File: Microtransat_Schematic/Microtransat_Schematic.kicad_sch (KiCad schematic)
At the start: 33 parts, among them IC1 HT7833, M12_Female2 LightTower1, U1 LM2596S-5, U10 RC_Reciever, U5 SD Card Module, U6 SEN0482 Wind Vane, U7 LoRa Module

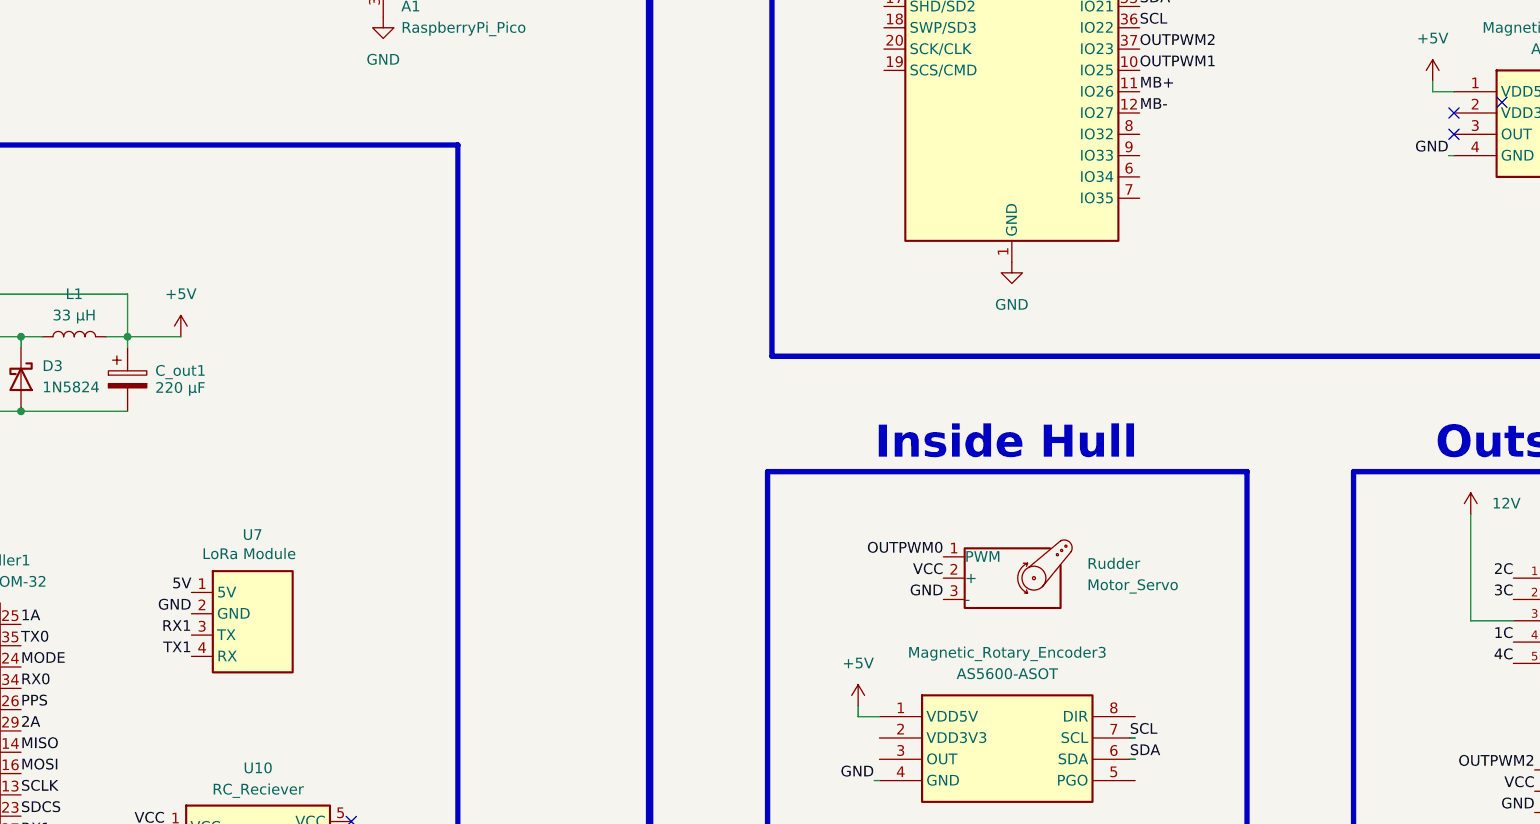
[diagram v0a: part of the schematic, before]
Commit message: Added AS5600 mockup
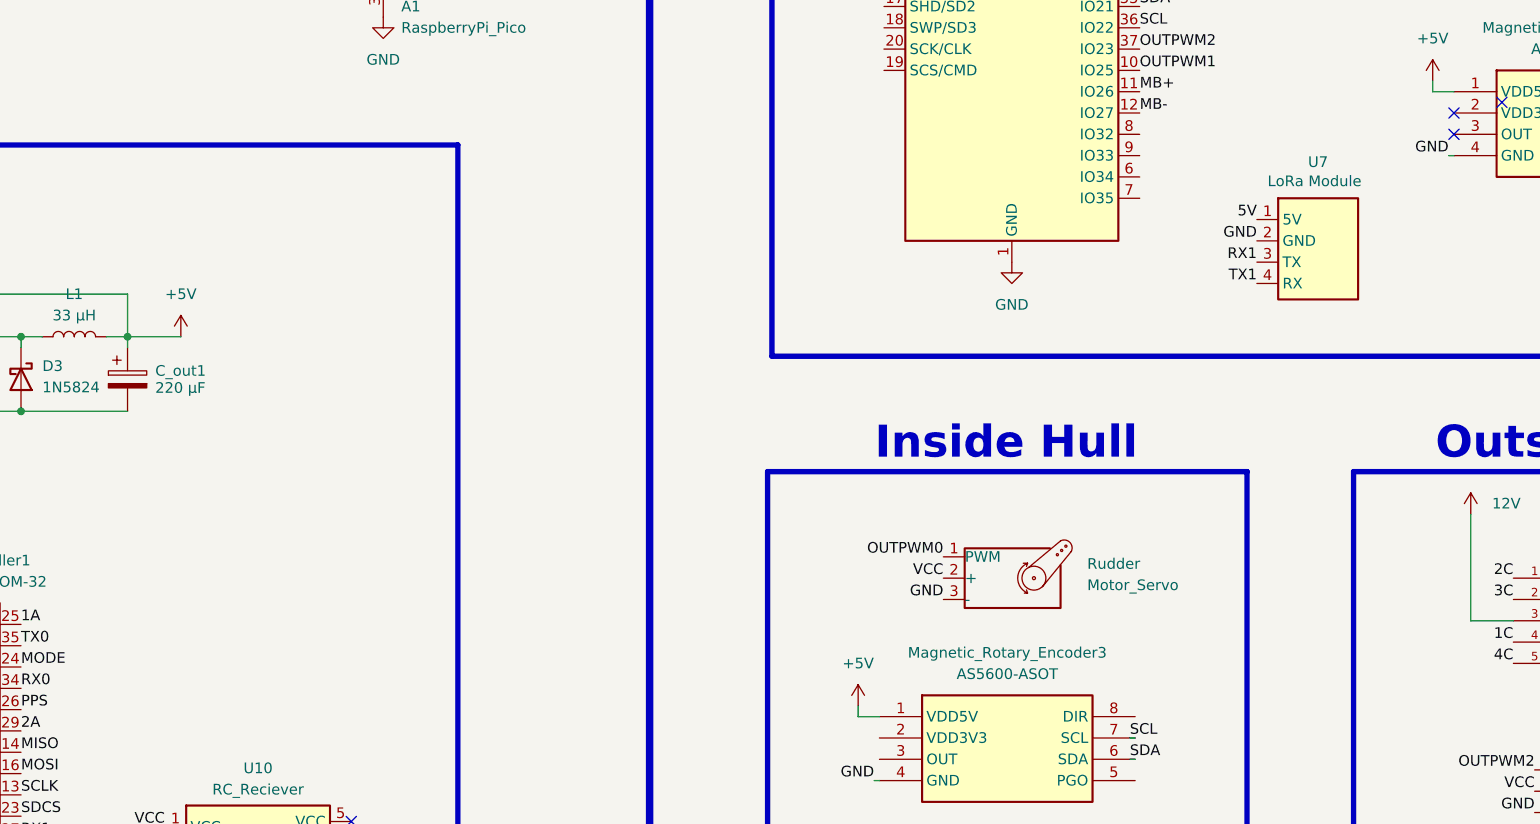
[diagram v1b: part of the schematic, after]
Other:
- moved on the sheet: U7
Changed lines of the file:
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@@
 	)
 	(label "TX1"
-		(at 187.96 193.04 180)
+		(at 314.96 148.59 180)
 		(effects
 			(font
@@
 	)
 	(label "5V"
-		(at 187.96 185.42 180)
+		(at 314.96 140.97 180)
 		(effects
 			(font
@@
 	)
 	(label "GND"
-		(at 187.96 187.96 180)
+		(at 314.96 143.51 180)
 		(effects
 			(font
@@
 	)
 	(label "RX1"
-		(at 187.96 190.5 180)
+		(at 314.96 146.05 180)
 		(effects
 			(font
@@
 	(symbol
 		(lib_id "Microtransat:LoRa Module")
-		(at 196.215 180.34 0)
+		(at 323.215 135.89 0)
 		(unit 1)
 		(exclude_from_sim no)
@@
 		(dnp no)
 		(property "Reference" "U7"
-			(at 194.056 178.562 0)
+			(at 321.056 134.112 0)
 			(effects
 				(font
@@
 		)
 		(property "Value" "LoRa Module"
-			(at 189.23 180.848 0)
+			(at 316.23 136.398 0)
 			(effects
 				(font
@@
 		)
 		(property "Footprint" ""
-			(at 196.215 180.34 0)
+			(at 323.215 135.89 0)
 			(effects
 				(font
@@
 		)
 		(property "Datasheet" ""
-			(at 196.215 180.34 0)
+			(at 323.215 135.89 0)
 			(effects
 				(font
@@
 		)
 		(property "Description" ""
-			(at 196.215 180.34 0)
+			(at 323.215 135.89 0)
 			(effects
 				(font

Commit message: Removed some old/incorrect stuff
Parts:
- removed C_in1: 680 µF, symbol Device:C_Polarized
- removed C_out1: 220 µF, symbol Device:C_Polarized
- removed D3: 1N5824, Diode_THT:D_DO-201AD_P15.24mm_Horizontal, symbol Diode:1N5820
- removed Gimbal: Motor_Servo, symbol Motor:Motor_Servo
- removed L1: 33 µH, symbol Device:L
- removed Logic_Shifter1: SN74AHCT125N, SN74AHCT125N:DIP794W45P254L1930H508Q14, symbol SN74AHCT125N:SN74AHCT125N
- removed U6: SEN0482 Wind Vane, symbol Microtransat:SEN0482 Wind Vane
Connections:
- net +5V: no longer U1.4 (FB)
- net 12V: no longer U1.1 (VIN)
- net GND: no longer U1.3 (GND), U1.5 (~{ON}/OFF)
- net MB+: no longer J1.4
- net MB-: no longer J1.5
- net OUTPWM1: no longer J1.3
- net at Tailwing.1 (PWM): no longer J1.9
- net at Tailwing.2 (+): no longer J1.7
- net at Tailwing.3 (-): no longer J1.8
- new net: U1.3 (GND), U1.5 (~{ON}/OFF)
- new net RX: J1.4
- new net TX: J1.3

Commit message: Added SD card footprint
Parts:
- U5: footprint (none) -> Adafruit 254:Adafruit_254
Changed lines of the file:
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@@
 			)
 		)
-		(property "Footprint" ""
+		(property "Footprint" "Adafruit 254:Adafruit_254"
 			(at 106.68 238.76 0)
 			(effects
